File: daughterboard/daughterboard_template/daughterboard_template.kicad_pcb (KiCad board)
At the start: 4 copper layers, 72 x 40 mm, 1 part, among them J1 PCIE-064-Daughterboard

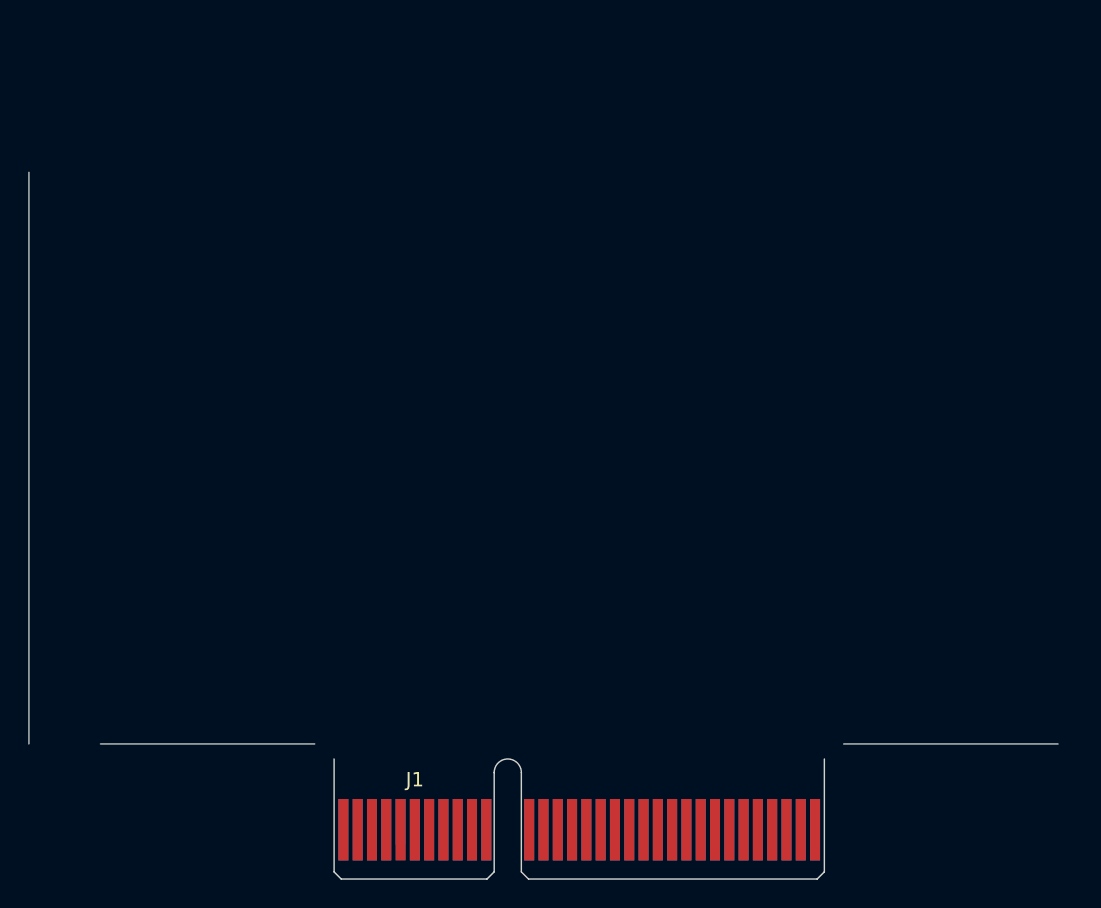
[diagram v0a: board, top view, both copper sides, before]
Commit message: finished daughterboard template layout
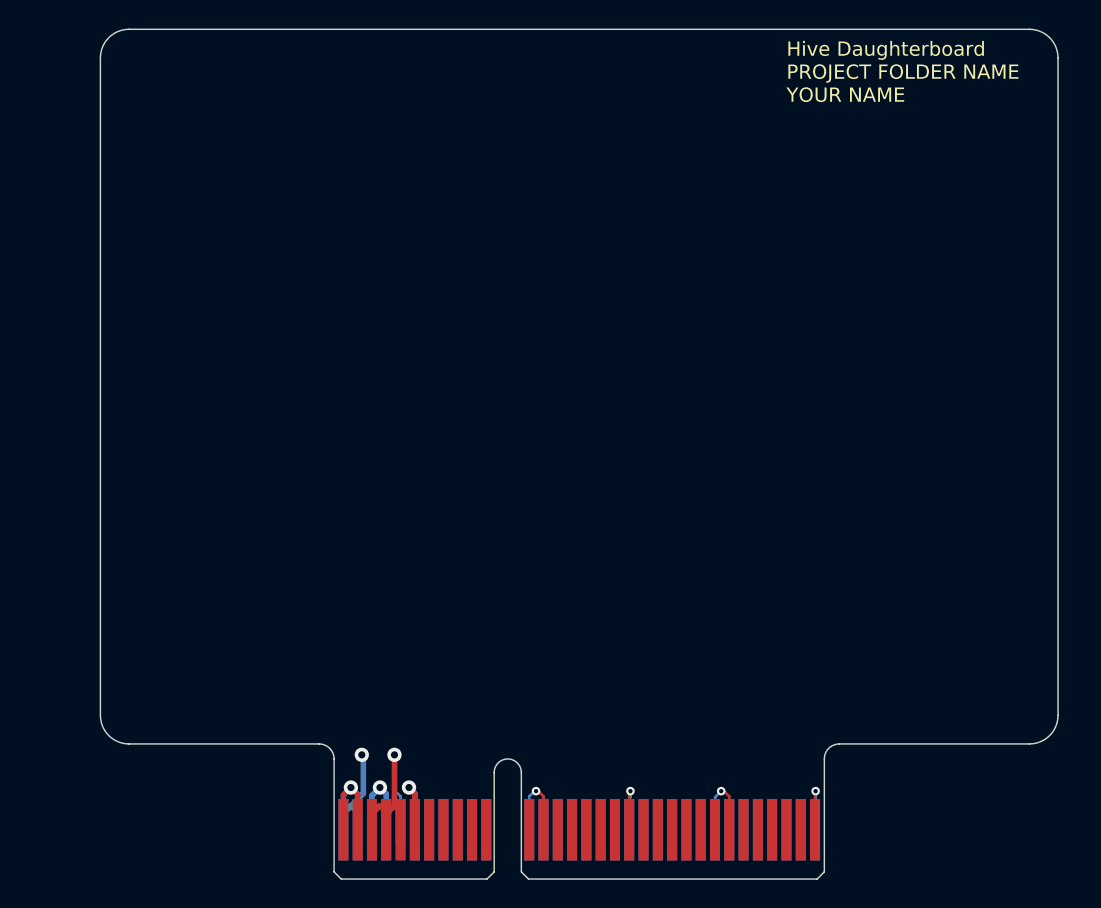
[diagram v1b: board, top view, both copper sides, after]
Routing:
- net GND: track 0.00 -> 41.7 mm, vias 0 -> 7
- net +3V3: track 0.00 -> 16.0 mm, vias 0 -> 1
- net +5V: track 0.00 -> 9.64 mm, vias 0 -> 1
- added copper zone on PWR_SIG.Cu, net +3V3
- added copper zone on GND.Cu, net GND
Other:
- board size 72 x 40 mm -> 67 x 51.1 mm
- net class Default: via_drill 0.4 -> 0.3
- net class Power added: clearance 0.3, trace_width 0.386, via_dia 1, via_drill 0.5
- net class Signal added: clearance 0.18, trace_width 0.18, via_dia 0.6, via_drill 0.3
- rule trace_min: 0.2 -> 0.152
- board text added: "Do not place any components inside the filled zone! Zone will be obscured by PCI connection"
- board text added: "Hive Daughterboard PROJECT FOLDER NAME YOUR NAME"
- board text added: "Outlined zone has a height clearance of max. 3mm on B.Cu Layer and max. 8mm on F.Cu layer"

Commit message: changed PCIE 64 to M.2 Key B connector
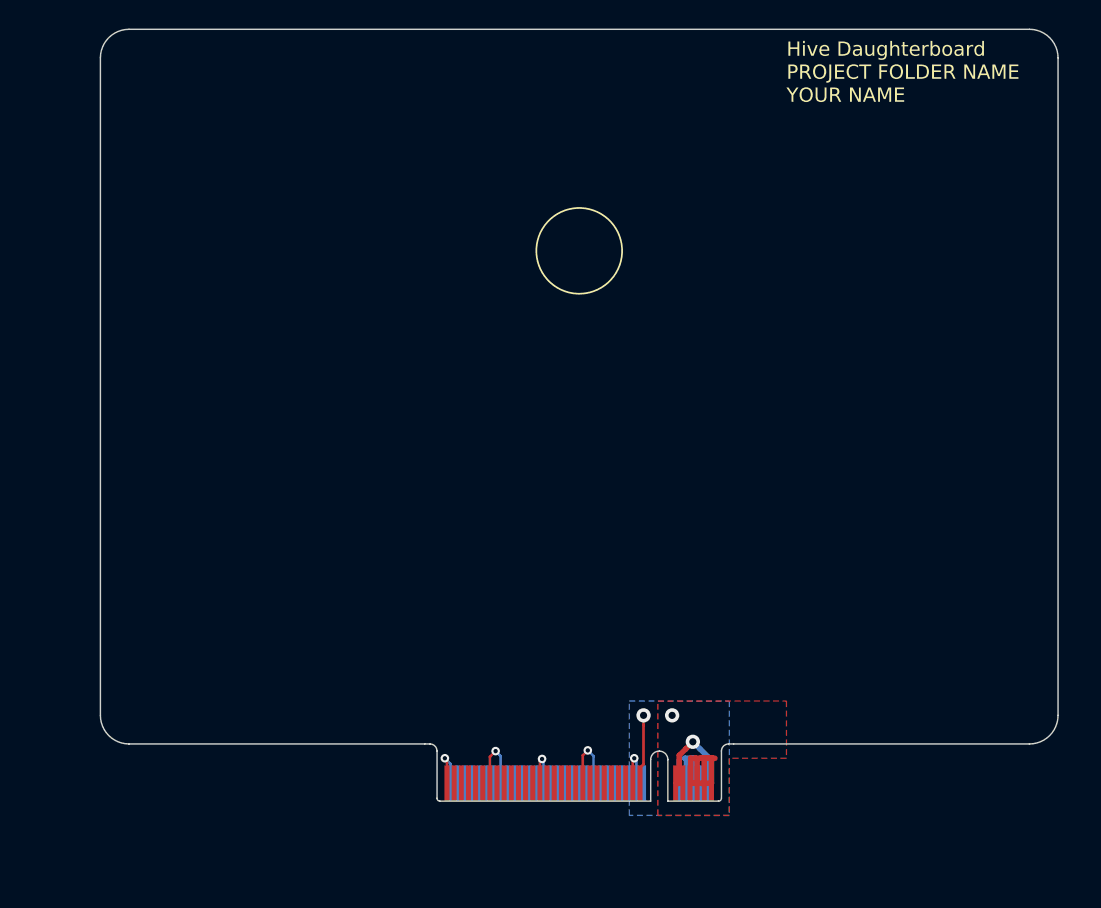
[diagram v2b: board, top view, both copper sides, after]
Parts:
- J1: value PCIE-064-Daughterboard -> m2_keyA_67pin_daughterboard; footprint hive:PCIexpress_x4_daughterboard -> hive:m2_keyB
- moved J1 16.6 mm to (148.5, 131.0)
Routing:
- net GND: track 41.7 -> 28.1 mm, vias 7 -> 6
- net +3V3: track 16.0 -> 11.6 mm, vias 1 -> 2
- net +5V: track 9.64 -> 11.6 mm, vias 1 -> 0
- added copper zone on B.Cu, net +3V3
- added copper zone on F.Cu, net +5V
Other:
- board size 67 x 51.1 mm -> 67 x 50 mm
- board text added: "Do not place any components inside the filled zone! Zone will be obscured by magnet"
- board text added: "Outlined zone has a height clearance of max. 1.28mm on B.Cu Layer and max. 8mm on F.Cu layer"
- board text added: "PCB Thickness 0.8mm"
- board text removed: "Outlined zone has a height clearance of max. 3mm on B.Cu Layer and max. 8mm on F.Cu layer"

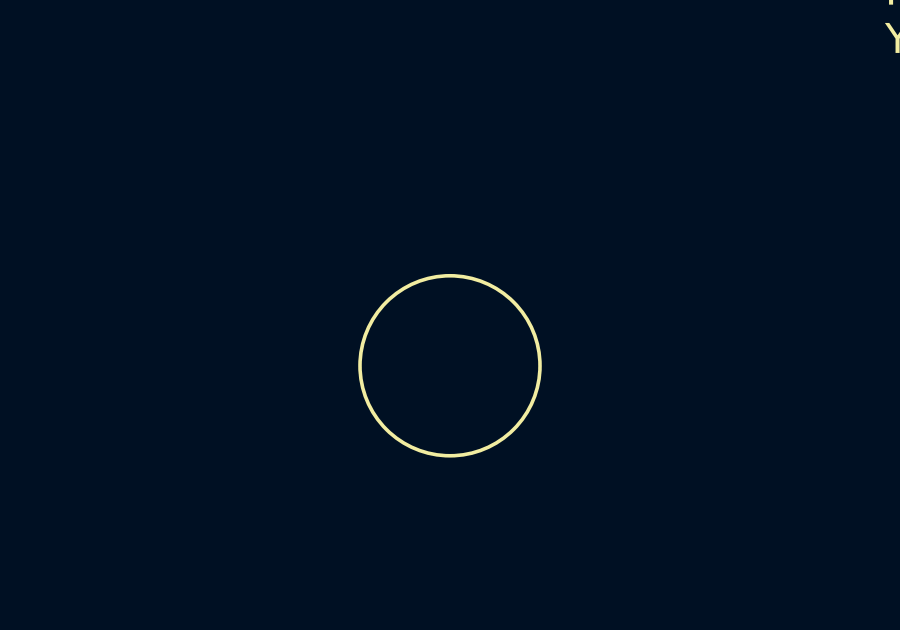
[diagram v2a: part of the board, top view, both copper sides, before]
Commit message: added M2.5 Daughterboard backup mounting solution
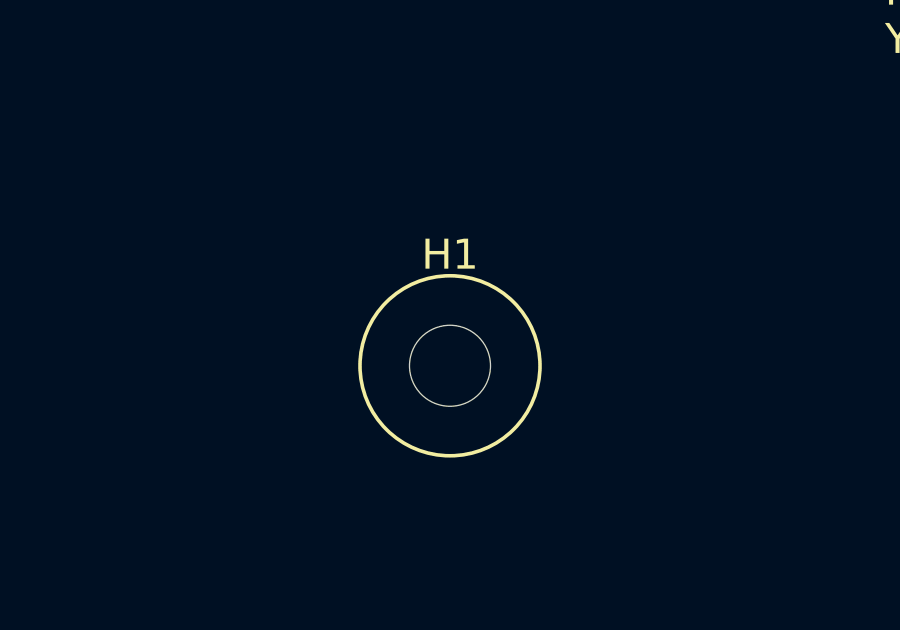
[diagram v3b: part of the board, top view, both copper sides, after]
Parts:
- added H1: MountingHoleDaughterboard, MountingHole:MountingHole_2.7mm_M2.5, F.Cu at (148.5, 92.5)
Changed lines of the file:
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@@
     (tracks 65)
     (zones 0)
-    (modules 1)
+    (modules 2)
     (nets 48)
   )
@@
     (add_net GND)
   )
+  (module MountingHole:MountingHole_2.7mm_M2.5 (layer F.Cu)
+    (at 148.5 92.5)
+    (descr "Mounting Hole 2.7mm, no annular, M2.5")
+    (tags "mounting hole 2.7mm no annular m2.5")
+    (attr virtual)
+    (fp_text reference H1 (at 0 -3.7) (layer F.SilkS)
+      (effects (font (size 1 1) (thickness 0.15)))
+    )
+    (fp_text value MountingHoleDaughterboard (at 0 3.7) (layer F.Fab)
+      (effects (font (size 1 1) (thickness 0.15)))
+    )
+    (fp_circle (center 0 0) (end 2.95 0) (layer F.CrtYd) (width 0.05))
+    (fp_circle (center 0 0) (end 2.7 0) (layer Cmts.User) (width 0.15))
+    (fp_text user %R (at 0.3 0) (layer F.Fab)
+      (effects (font (size 1 1) (thickness 0.15)))
+    )
+    (pad 1 np_thru_hole circle (at 0 0) (size 2.7 2.7) (drill 2.7) (layers *.Cu *.Mask))
+  )
   (module hive:m2_keyB (layer F.Cu)
     (at 148.5 131)
@@
   (segment (start 156.45 128) (end 155.886 128) (width 0.386) (layer B.Cu) (net 43))
   (segment (start 155.5 129.75) (end 155.5 128.114) (width 0.386) (layer B.Cu) (net 43))
+  (via (at 155 125) (size 1) (drill 0.5) (layers F.Cu B.Cu) (net 43))
+  (segment (start 153 128.425) (end 153 125.707106) (width 0.18) (layer F.Cu) (net 43))
+  (segment (start 152.75 128.675) (end 153 128.425) (width 0.18) (layer F.Cu) (net 43))
+  (segment (start 153 125.707106) (end 153 125) (width 0.18) (layer F.Cu) (net 43))
+  (segment (start 152.75 129.75) (end 152.75 128.675) (width 0.18) (layer F.Cu) (net 43))
   (segment (start 157.75 129.75) (end 156.298001 129.75) (width 0.386) (layer F.Cu) (net 44))
   (segment (start 157.25 128.114) (end 157.364 128) (width 0.386) (layer F.Cu) (net 44))
@@
   (segment (start 156.636 128) (end 156.298001 128) (width 0.386) (layer F.Cu) (net 44))
   (segment (start 156.75 129.75) (end 156.298001 129.75) (width 0.386) (layer F.Cu) (net 44))
-  (via (at 155 125) (size 1) (drill 0.5) (layers F.Cu B.Cu) (net 43))
-  (segment (start 153 128.425) (end 153 125.707106) (width 0.18) (layer F.Cu) (net 43))
-  (segment (start 152.75 128.675) (end 153 128.425) (width 0.18) (layer F.Cu) (net 43))
-  (segment (start 153 125.707106) (end 153 125) (width 0.18) (layer F.Cu) (net 43))
-  (segment (start 152.75 129.75) (end 152.75 128.675) (width 0.18) (layer F.Cu) (net 43))
   (zone (net 1) (net_name GND) (layer GND.Cu) (hatch edge 0.508)
     (connect_pads (clearance 0.2))

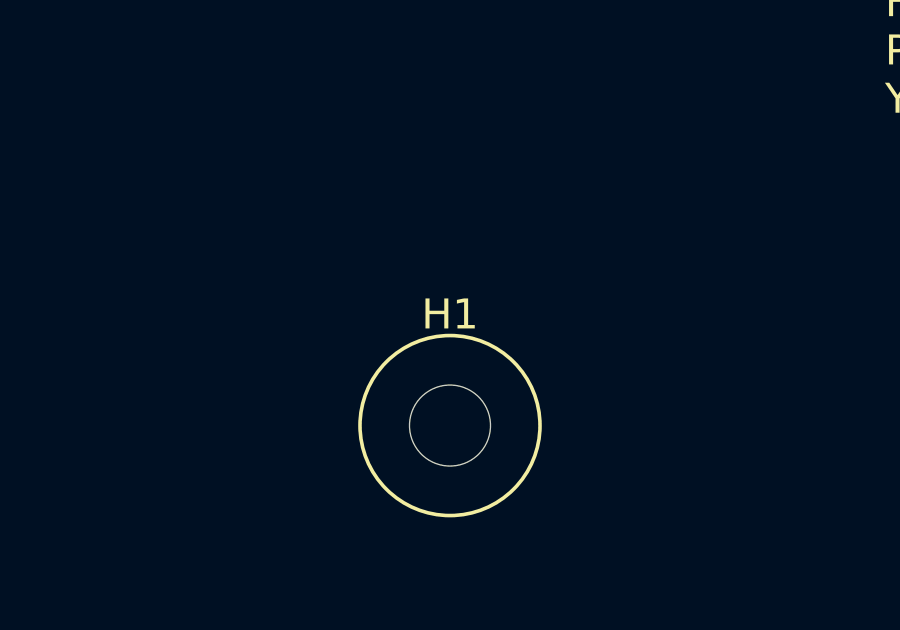
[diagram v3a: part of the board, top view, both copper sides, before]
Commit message: added project library to daughterboard template + minor pcb adjustments
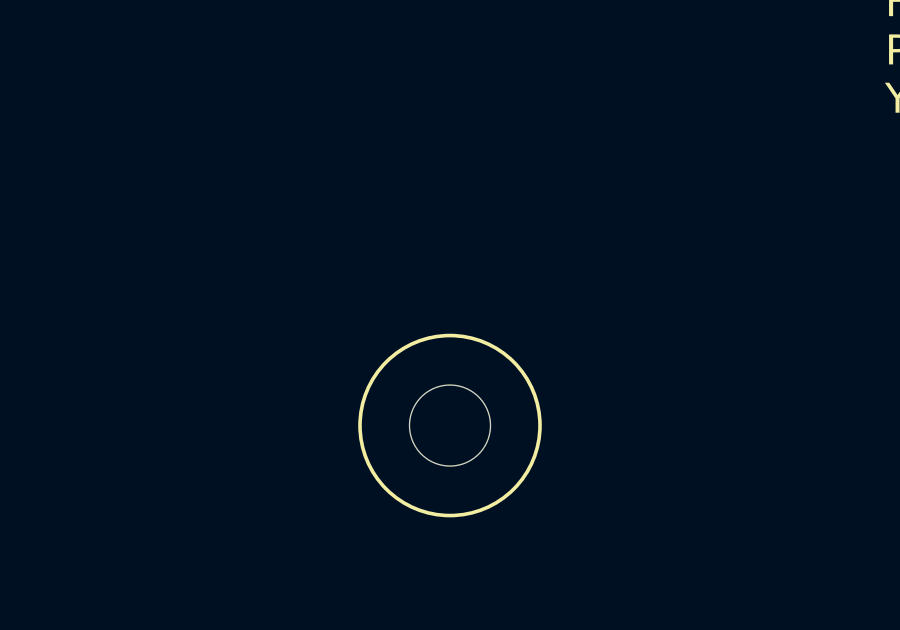
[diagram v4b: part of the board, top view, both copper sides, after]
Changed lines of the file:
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@@
     (tags "mounting hole 2.7mm no annular m2.5")
     (attr virtual)
-    (fp_text reference H1 (at 0 -3.7) (layer F.SilkS)
+    (fp_text reference H1 (at 0 -3.7) (layer F.SilkS) hide
       (effects (font (size 1 1) (thickness 0.15)))
     )
-    (fp_text value MountingHoleDaughterboard (at 0 3.7) (layer F.Fab)
+    (fp_text value MountingHoleDaughterboard (at 0 3.7) (layer F.Fab) hide
       (effects (font (size 1 1) (thickness 0.15)))
     )
